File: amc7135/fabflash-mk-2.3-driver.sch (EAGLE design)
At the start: 14 parts, among them U1 TINY85, U2 AMC7135SOT-89, U3 AMC7135SOT-89, U4 AMC7135SOT-89, U5 AMC7135SOT-89

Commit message: slowly making progress toward a buildable device
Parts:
- removed +, 5V, B-, G-, R-, W-: M01SMD_2X3MM, A_butts:M01SMD_2X3MM
- removed C1: 10uF, A_butts:CAPACITOR-CERAMICC0805
- removed GND: M01NOT-A-VIA-NOPE, A_butts:M01NOT-A-VIA-NOPE
- removed R1: 100k, A_butts:RESISTORR0805
- removed U1: TINY85, A_butts:ATTINY45TINY85-20-QFN
- added JP1: (no value), A_butts:M05JST-PH-RA-PTH
- added JP2, JP3, JP4, JP5, JP6, JP7: M01PTH-0.9MM-NS, A_butts:M01PTH-0.9MM-NS
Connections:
- removed net 5V: +.1, 5V.1, C1.1, R1.1, U1.VCC
- removed net N$1: R1.2, U1.RESET
- new net +: JP1.1, JP6.1
- net BLUE-: now also JP1.3; no longer B-.1
- net BLUEPWM: now also JP4.1; no longer U1.PB1(MISO)
- net GND: now also JP7.1; no longer C1.2, GND.1, U1.GND
- net GREEN-: now also JP1.4; no longer G-.1
- net GREENPWM: now also JP3.1; no longer U1.PB4(ADC2)
- net RED-: now also JP1.5; no longer R-.1
- net REDPWM: now also JP2.1; no longer U1.PB3(ADC3)
- net WHITE-: now also JP1.2; no longer W-.1
- net WHITEPWM: now also JP5.1; no longer U1.PB0(MOSI)

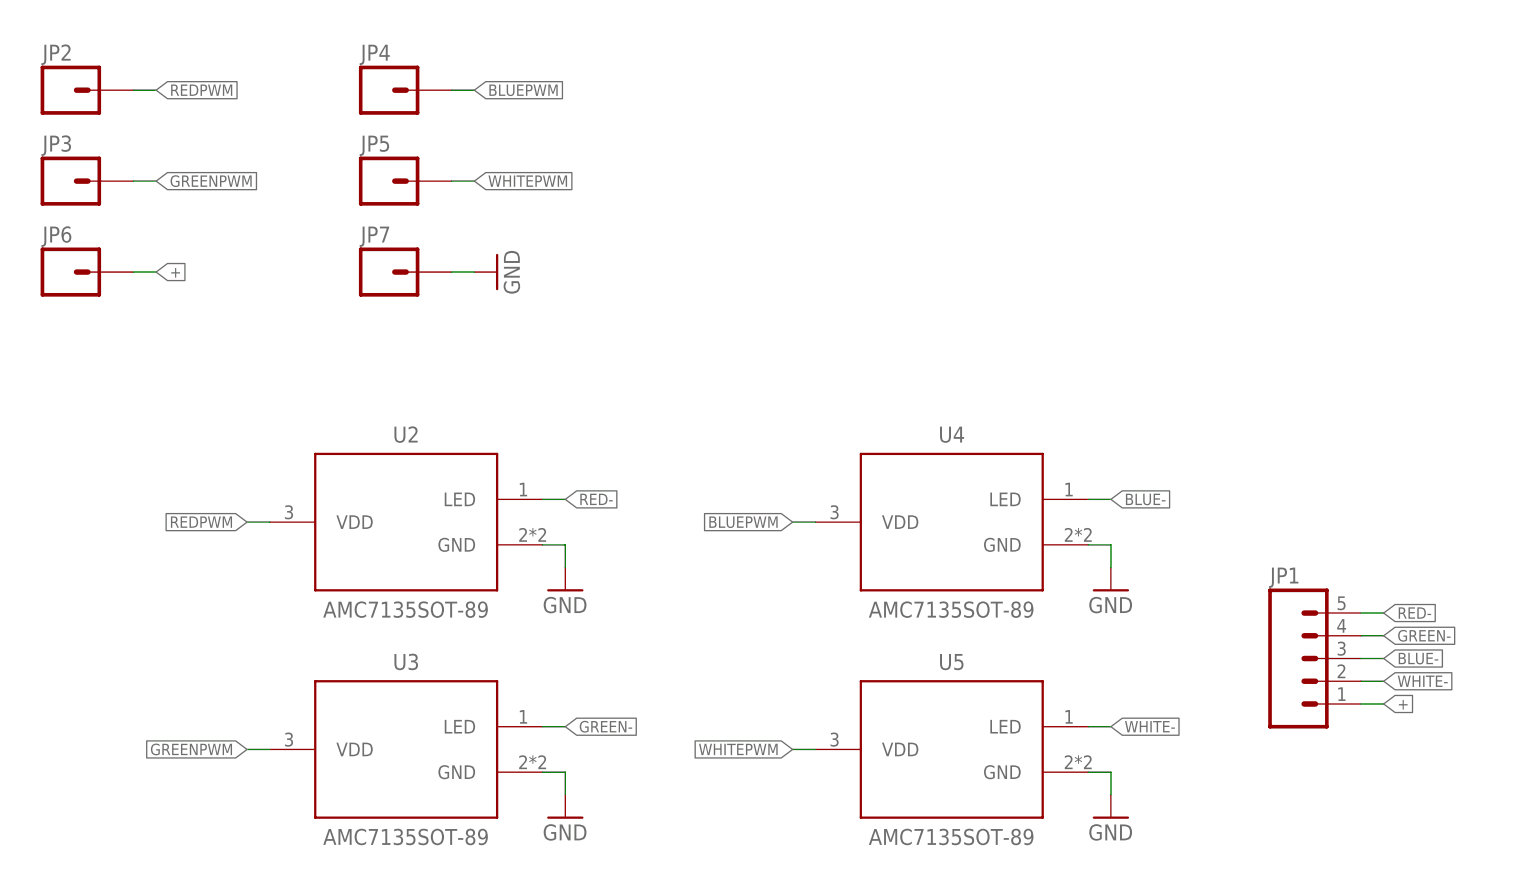
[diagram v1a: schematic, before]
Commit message: added #2 screw holes to each board and verified pins aligned correctly (had to flipflop 5v/gnd a few times)
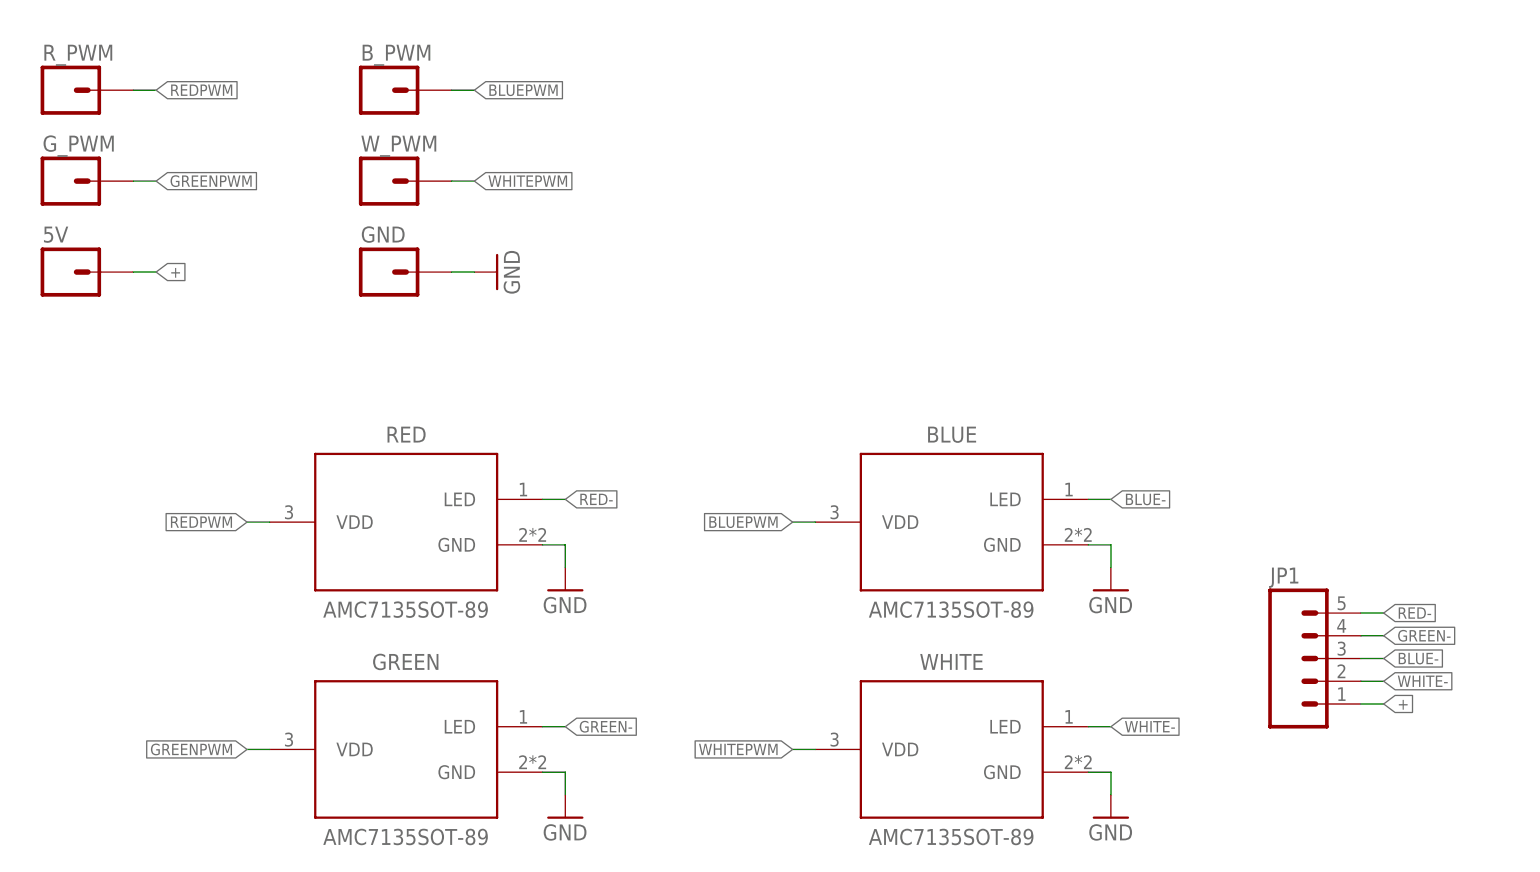
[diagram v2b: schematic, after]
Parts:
- removed JP2, JP3, JP4, JP5, JP6, JP7: M01PTH-0.9MM-NS, A_butts:M01PTH-0.9MM-NS
- added 5V, B_PWM, GND, G_PWM, R_PWM, W_PWM: M01PTH-0.9MM, A_butts:M01PTH-0.9MM
- renumbered U2 to RED, U3 to GREEN, U4 to BLUE, U5 to WHITE
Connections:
- net +: now also 5V.1; no longer JP6.1
- net BLUEPWM: now also B_PWM.1; no longer JP4.1
- net GND: now also GND.1; no longer JP7.1
- net GREENPWM: now also G_PWM.1; no longer JP3.1
- net REDPWM: now also R_PWM.1; no longer JP2.1
- net WHITEPWM: now also W_PWM.1; no longer JP5.1
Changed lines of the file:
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@@
 <part name="GND2" library="A_butts" deviceset="GND" device=""/>
 <part name="GND3" library="A_butts" deviceset="GND" device=""/>
-<part name="U2" library="A_butts" deviceset="AMC7135" device="SOT-89"/>
-<part name="U3" library="A_butts" deviceset="AMC7135" device="SOT-89"/>
-<part name="U4" library="A_butts" deviceset="AMC7135" device="SOT-89"/>
+<part name="RED" library="A_butts" deviceset="AMC7135" device="SOT-89"/>
+<part name="GREEN" library="A_butts" deviceset="AMC7135" device="SOT-89"/>
+<part name="BLUE" library="A_butts" deviceset="AMC7135" device="SOT-89"/>
 <part name="GND1" library="A_butts" deviceset="GND" device=""/>
 <part name="GND7" library="A_butts" deviceset="GND" device=""/>
-<part name="U5" library="A_butts" deviceset="AMC7135" device="SOT-89"/>
+<part name="WHITE" library="A_butts" deviceset="AMC7135" device="SOT-89"/>
 <part name="JP1" library="A_butts" deviceset="M05" device="JST-PH-RA-PTH"/>
 <part name="GND4" library="A_butts" deviceset="GND" device=""/>
-<part name="JP2" library="A_butts" deviceset="M01" device="PTH-0.9MM-NS" value="M01PTH-0.9MM-NS"/>
-<part name="JP3" library="A_butts" deviceset="M01" device="PTH-0.9MM-NS" value="M01PTH-0.9MM-NS"/>
-<part name="JP4" library="A_butts" deviceset="M01" device="PTH-0.9MM-NS" value="M01PTH-0.9MM-NS"/>
-<part name="JP5" library="A_butts" deviceset="M01" device="PTH-0.9MM-NS" value="M01PTH-0.9MM-NS"/>
-<part name="JP6" library="A_butts" deviceset="M01" device="PTH-0.9MM-NS" value="M01PTH-0.9MM-NS"/>
-<part name="JP7" library="A_butts" deviceset="M01" device="PTH-0.9MM-NS" value="M01PTH-0.9MM-NS"/>
+<part name="R_PWM" library="A_butts" deviceset="M01" device="PTH-0.9MM" value="M01PTH-0.9MM"/>
+<part name="G_PWM" library="A_butts" deviceset="M01" device="PTH-0.9MM" value="M01PTH-0.9MM"/>
+<part name="B_PWM" library="A_butts" deviceset="M01" device="PTH-0.9MM" value="M01PTH-0.9MM"/>
+<part name="W_PWM" library="A_butts" deviceset="M01" device="PTH-0.9MM" value="M01PTH-0.9MM"/>
+<part name="5V" library="A_butts" deviceset="M01" device="PTH-0.9MM" value="M01PTH-0.9MM"/>
+<part name="GND" library="A_butts" deviceset="M01" device="PTH-0.9MM" value="M01PTH-0.9MM"/>
 </parts>
 <sheets>
@@
 <instance part="GND2" gate="1" x="58.42" y="53.34"/>
 <instance part="GND3" gate="1" x="119.38" y="78.74"/>
-<instance part="U2" gate="G$1" x="40.64" y="86.36"/>
-<instance part="U3" gate="G$1" x="40.64" y="60.96"/>
-<instance part="U4" gate="G$1" x="101.6" y="86.36"/>
+<instance part="RED" gate="G$1" x="40.64" y="86.36"/>
+<instance part="GREEN" gate="G$1" x="40.64" y="60.96"/>
+<instance part="BLUE" gate="G$1" x="101.6" y="86.36"/>
 <instance part="GND1" gate="1" x="58.42" y="78.74"/>
 <instance part="GND7" gate="1" x="119.38" y="53.34"/>
-<instance part="U5" gate="G$1" x="101.6" y="60.96"/>
+<instance part="WHITE" gate="G$1" x="101.6" y="60.96"/>
 <instance part="JP1" gate="G$1" x="139.7" y="71.12"/>
 <instance part="GND4" gate="1" x="50.8" y="114.3" rot="R90"/>
-<instance part="JP2" gate="G$1" x="2.54" y="134.62"/>
-<instance part="JP3" gate="G$1" x="2.54" y="124.46"/>
-<instance part="JP4" gate="G$1" x="38.1" y="134.62"/>
-<instance part="JP5" gate="G$1" x="38.1" y="124.46"/>
-<instance part="JP6" gate="G$1" x="2.54" y="114.3"/>
-<instance part="JP7" gate="G$1" x="38.1" y="114.3"/>
+<instance part="R_PWM" gate="G$1" x="2.54" y="134.62"/>
+<instance part="G_PWM" gate="G$1" x="2.54" y="124.46"/>
+<instance part="B_PWM" gate="G$1" x="38.1" y="134.62"/>
+<instance part="W_PWM" gate="G$1" x="38.1" y="124.46"/>
+<instance part="5V" gate="G$1" x="2.54" y="114.3"/>
+<instance part="GND" gate="G$1" x="38.1" y="114.3"/>
 </instances>
 <busses>
@@
 <net name="GND" class="0">
 <segment>
-<pinref part="U2" gate="G$1" pin="GND"/>
+<pinref part="RED" gate="G$1" pin="GND"/>
 <wire x1="55.88" y1="83.82" x2="58.42" y2="83.82" width="0.1524" layer="91"/>
 <pinref part="GND1" gate="1" pin="GND"/>
@@
 </segment>
 <segment>
-<pinref part="U3" gate="G$1" pin="GND"/>
+<pinref part="GREEN" gate="G$1" pin="GND"/>
 <wire x1="55.88" y1="58.42" x2="58.42" y2="58.42" width="0.1524" layer="91"/>
 <pinref part="GND2" gate="1" pin="GND"/>
@@
 </segment>
 <segment>
-<pinref part="U4" gate="G$1" pin="GND"/>
+<pinref part="BLUE" gate="G$1" pin="GND"/>
 <wire x1="116.84" y1="83.82" x2="119.38" y2="83.82" width="0.1524" layer="91"/>
 <pinref part="GND3" gate="1" pin="GND"/>
@@
 </segment>
 <segment>
-<pinref part="U5" gate="G$1" pin="GND"/>
+<pinref part="WHITE" gate="G$1" pin="GND"/>
 <wire x1="116.84" y1="58.42" x2="119.38" y2="58.42" width="0.1524" layer="91"/>
 <pinref part="GND7" gate="1" pin="GND"/>
@@
 <pinref part="GND4" gate="1" pin="GND"/>
 <wire x1="45.72" y1="114.3" x2="48.26" y2="114.3" width="0.1524" layer="91"/>
-<pinref part="JP7" gate="G$1" pin="1"/>
+<pinref part="GND" gate="G$1" pin="1"/>
 </segment>
 </net>
 <net name="GREENPWM" class="0">
 <segment>
-<pinref part="U3" gate="G$1" pin="VDD"/>
+<pinref part="GREEN" gate="G$1" pin="VDD"/>
 <wire x1="25.4" y1="60.96" x2="22.86" y2="60.96" width="0.1524" layer="91"/>
 <label x="22.86" y="60.96" size="1.27" layer="95" rot="R180" xref="yes"/>
@@
 <wire x1="12.7" y1="124.46" x2="10.16" y2="124.46" width="0.1524" layer="91"/>
 <label x="12.7" y="124.46" size="1.27" layer="95" xref="yes"/>
-<pinref part="JP3" gate="G$1" pin="1"/>
+<pinref part="G_PWM" gate="G$1" pin="1"/>
 </segment>
 </net>
 <net name="REDPWM" class="0">
 <segment>
-<pinref part="U2" gate="G$1" pin="VDD"/>
+<pinref part="RED" gate="G$1" pin="VDD"/>
 <wire x1="25.4" y1="86.36" x2="22.86" y2="86.36" width="0.1524" layer="91"/>
 <label x="22.86" y="86.36" size="1.27" layer="95" rot="R180" xref="yes"/>
@@
 <wire x1="12.7" y1="134.62" x2="10.16" y2="134.62" width="0.1524" layer="91"/>
 <label x="12.7" y="134.62" size="1.27" layer="95" xref="yes"/>
-<pinref part="JP2" gate="G$1" pin="1"/>
+<pinref part="R_PWM" gate="G$1" pin="1"/>
 </segment>
 </net>
 <net name="BLUE-" class="0">
 <segment>
-<pinref part="U4" gate="G$1" pin="LED"/>
+<pinref part="BLUE" gate="G$1" pin="LED"/>
 <wire x1="116.84" y1="88.9" x2="119.38" y2="88.9" width="0.1524" layer="91"/>
 <label x="119.38" y="88.9" size="1.27" layer="95" xref="yes"/>
@@
 <net name="GREEN-" class="0">
 <segment>
-<pinref part="U3" gate="G$1" pin="LED"/>
+<pinref part="GREEN" gate="G$1" pin="LED"/>
 <wire x1="55.88" y1="63.5" x2="58.42" y2="63.5" width="0.1524" layer="91"/>
 <label x="58.42" y="63.5" size="1.27" layer="95" xref="yes"/>
@@
 <net name="BLUEPWM" class="0">
 <segment>
-<pinref part="U4" gate="G$1" pin="VDD"/>
+<pinref part="BLUE" gate="G$1" pin="VDD"/>
 <wire x1="86.36" y1="86.36" x2="83.82" y2="86.36" width="0.1524" layer="91"/>
 <label x="83.82" y="86.36" size="1.27" layer="95" rot="R180" xref="yes"/>
@@
 <wire x1="48.26" y1="134.62" x2="45.72" y2="134.62" width="0.1524" layer="91"/>
 <label x="48.26" y="134.62" size="1.27" layer="95" xref="yes"/>
-<pinref part="JP4" gate="G$1" pin="1"/>
+<pinref part="B_PWM" gate="G$1" pin="1"/>
 </segment>
 </net>
 <net name="RED-" class="0">
 <segment>
-<pinref part="U2" gate="G$1" pin="LED"/>
+<pinref part="RED" gate="G$1" pin="LED"/>
 <wire x1="55.88" y1="88.9" x2="58.42" y2="88.9" width="0.1524" layer="91"/>
 <label x="58.42" y="88.9" size="1.27" layer="95" xref="yes"/>
@@
 <net name="WHITEPWM" class="0">
 <segment>
-<pinref part="U5" gate="G$1" pin="VDD"/>
+<pinref part="WHITE" gate="G$1" pin="VDD"/>
 <wire x1="86.36" y1="60.96" x2="83.82" y2="60.96" width="0.1524" layer="91"/>
 <label x="83.82" y="60.96" size="1.27" layer="95" rot="R180" xref="yes"/>
@@
 <wire x1="48.26" y1="124.46" x2="45.72" y2="124.46" width="0.1524" layer="91"/>
 <label x="48.26" y="124.46" size="1.27" layer="95" xref="yes"/>
-<pinref part="JP5" gate="G$1" pin="1"/>
+<pinref part="W_PWM" gate="G$1" pin="1"/>
 </segment>
 </net>
 <net name="WHITE-" class="0">
 <segment>
-<pinref part="U5" gate="G$1" pin="LED"/>
+<pinref part="WHITE" gate="G$1" pin="LED"/>
 <wire x1="116.84" y1="63.5" x2="119.38" y2="63.5" width="0.1524" layer="91"/>
 <label x="119.38" y="63.5" size="1.27" layer="95" xref="yes"/>
@@
 <wire x1="12.7" y1="114.3" x2="10.16" y2="114.3" width="0.1524" layer="91"/>
 <label x="12.7" y="114.3" size="1.27" layer="95" xref="yes"/>
-<pinref part="JP6" gate="G$1" pin="1"/>
+<pinref part="5V" gate="G$1" pin="1"/>
 </segment>
 </net>

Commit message: finishing touches hopefully
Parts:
- JP1: value (none) -> M05JST-PH-RA-PTH
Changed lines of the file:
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@@
 <grid distance="100" unitdist="mil" unit="mil" style="lines" multiple="1" display="yes" altdistance="1" altunitdist="mm" altunit="mm"/>
 <layers>
-<layer number="1" name="Top" color="4" fill="1" visible="yes" active="no"/>
-<layer number="16" name="Bottom" color="1" fill="1" visible="yes" active="no"/>
-<layer number="17" name="Pads" color="2" fill="1" visible="yes" active="no"/>
-<layer number="18" name="Vias" color="2" fill="1" visible="yes" active="no"/>
-<layer number="19" name="Unrouted" color="6" fill="1" visible="yes" active="no"/>
-<layer number="20" name="Dimension" color="15" fill="1" visible="yes" active="no"/>
-<layer number="21" name="tPlace" color="7" fill="1" visible="yes" active="no"/>
-<layer number="22" name="bPlace" color="7" fill="1" visible="yes" active="no"/>
-<layer number="23" name="tOrigins" color="15" fill="1" visible="yes" active="no"/>
-<layer number="24" name="bOrigins" color="15" fill="1" visible="yes" active="no"/>
-<layer number="25" name="tNames" color="7" fill="1" visible="yes" active="no"/>
-<layer number="26" name="bNames" color="7" fill="1" visible="yes" active="no"/>
-<layer number="27" name="tValues" color="7" fill="1" visible="yes" active="no"/>
-<layer number="28" name="bValues" color="7" fill="1" visible="yes" active="no"/>
+<layer number="1" name="Top" color="4" fill="1" visible="no" active="no"/>
+<layer number="16" name="Bottom" color="1" fill="1" visible="no" active="no"/>
+<layer number="17" name="Pads" color="2" fill="1" visible="no" active="no"/>
+<layer number="18" name="Vias" color="2" fill="1" visible="no" active="no"/>
+<layer number="19" name="Unrouted" color="6" fill="1" visible="no" active="no"/>
+<layer number="20" name="Dimension" color="15" fill="1" visible="no" active="no"/>
+<layer number="21" name="tPlace" color="7" fill="1" visible="no" active="no"/>
+<layer number="22" name="bPlace" color="7" fill="1" visible="no" active="no"/>
+<layer number="23" name="tOrigins" color="15" fill="1" visible="no" active="no"/>
+<layer number="24" name="bOrigins" color="15" fill="1" visible="no" active="no"/>
+<layer number="25" name="tNames" color="7" fill="1" visible="no" active="no"/>
+<layer number="26" name="bNames" color="7" fill="1" visible="no" active="no"/>
+<layer number="27" name="tValues" color="7" fill="1" visible="no" active="no"/>
+<layer number="28" name="bValues" color="7" fill="1" visible="no" active="no"/>
 <layer number="29" name="tStop" color="7" fill="3" visible="no" active="no"/>
 <layer number="30" name="bStop" color="7" fill="6" visible="no" active="no"/>
@@
 <layer number="35" name="tGlue" color="7" fill="4" visible="no" active="no"/>
 <layer number="36" name="bGlue" color="7" fill="5" visible="no" active="no"/>
-<layer number="37" name="tTest" color="7" fill="1" visible="yes" active="no"/>
-<layer number="38" name="bTest" color="7" fill="1" visible="yes" active="no"/>
+<layer number="37" name="tTest" color="7" fill="1" visible="no" active="no"/>
+<layer number="38" name="bTest" color="7" fill="1" visible="no" active="no"/>
 <layer number="39" name="tKeepout" color="4" fill="11" visible="no" active="no"/>
 <layer number="40" name="bKeepout" color="1" fill="11" visible="no" active="no"/>
@@
 <layer number="44" name="Drills" color="7" fill="1" visible="no" active="no"/>
 <layer number="45" name="Holes" color="7" fill="1" visible="no" active="no"/>
-<layer number="46" name="Milling" color="3" fill="1" visible="yes" active="no"/>
-<layer number="47" name="Measures" color="7" fill="1" visible="yes" active="no"/>
-<layer number="48" name="Document" color="7" fill="1" visible="yes" active="no"/>
-<layer number="49" name="Reference" color="7" fill="1" visible="yes" active="no"/>
-<layer number="50" name="dxf" color="7" fill="1" visible="yes" active="no"/>
-<layer number="51" name="tDocu" color="7" fill="1" visible="yes" active="no"/>
-<layer number="52" name="bDocu" color="7" fill="1" visible="yes" active="no"/>
-<layer number="53" name="tGND_GNDA" color="7" fill="9" visible="yes" active="no"/>
-<layer number="54" name="bGND_GNDA" color="1" fill="9" visible="yes" active="no"/>
-<layer number="56" name="wert" color="7" fill="1" visible="yes" active="no"/>
-<layer number="57" name="tCAD" color="7" fill="1" visible="yes" active="no"/>
+<layer number="46" name="Milling" color="3" fill="1" visible="no" active="no"/>
+<layer number="47" name="Measures" color="7" fill="1" visible="no" active="no"/>
+<layer number="48" name="Document" color="7" fill="1" visible="no" active="no"/>
+<layer number="49" name="Reference" color="7" fill="1" visible="no" active="no"/>
+<layer number="50" name="dxf" color="7" fill="1" visible="no" active="no"/>
+<layer number="51" name="tDocu" color="7" fill="1" visible="no" active="no"/>
+<layer number="52" name="bDocu" color="7" fill="1" visible="no" active="no"/>
+<layer number="53" name="tGND_GNDA" color="7" fill="9" visible="no" active="no"/>
+<layer number="54" name="bGND_GNDA" color="1" fill="9" visible="no" active="no"/>
+<layer number="56" name="wert" color="7" fill="1" visible="no" active="no"/>
+<layer number="57" name="tCAD" color="7" fill="1" visible="no" active="no"/>
 <layer number="91" name="Nets" color="2" fill="1" visible="yes" active="yes"/>
 <layer number="92" name="Busses" color="1" fill="1" visible="yes" active="yes"/>
